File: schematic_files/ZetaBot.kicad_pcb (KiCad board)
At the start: 2 copper layers, 241.5 x 110.5 mm, 17 parts, among them J1 USB C PD Modulle, J2 Conn_01x05, J3 MOTOR_L, J4 MOTOR_R, SW1 SW_SPDT, U1 RPI5, U1 RPLIDAR C1, U2 Buck Converter

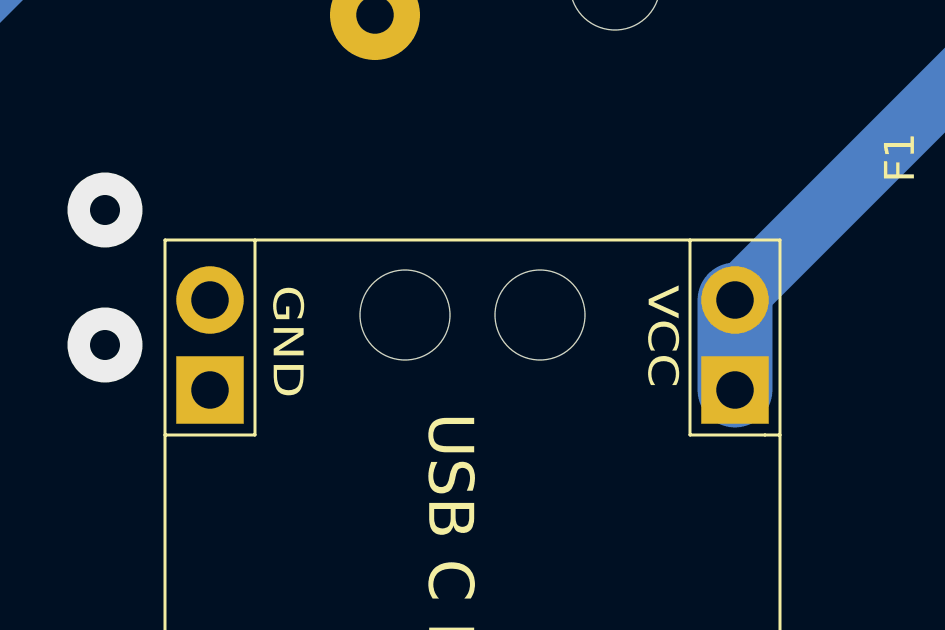
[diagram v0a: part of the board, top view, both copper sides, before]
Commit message: Added a new footprint for the USB C PD.
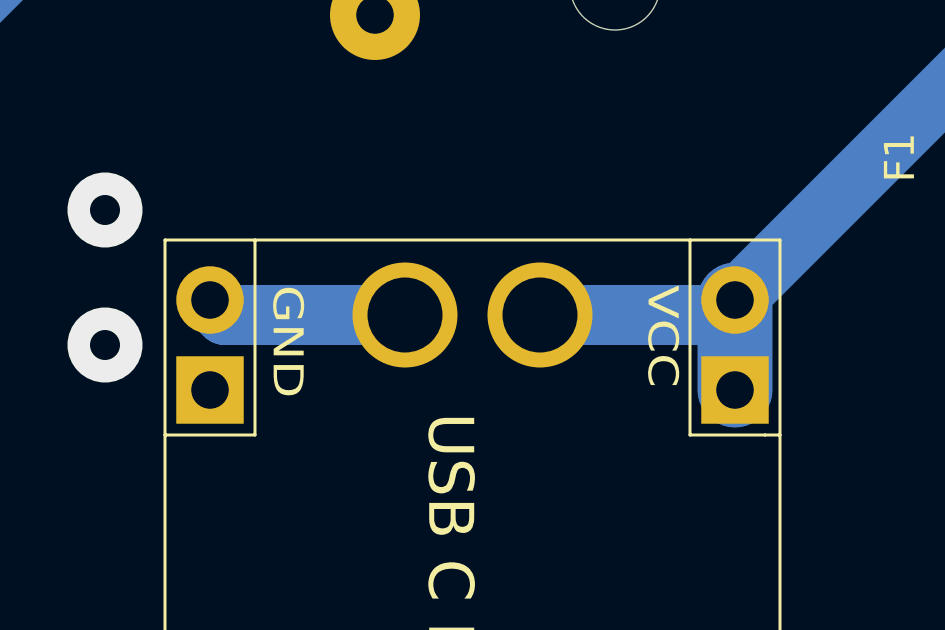
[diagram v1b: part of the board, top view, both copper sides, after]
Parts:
- J1: footprint deltabot:USB_C -> DeltaBotFootprints:USB_C
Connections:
- F1 pad 2: Net-(J1-VCC) -> Net-(F1-Pad2)
- J1 pad 1: Net-(J1-VCC) -> Net-(F1-Pad2)
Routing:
- net Net-(F1-Pad2): track 0.00 -> 27.9 mm
- net Net-(J1-VCC): track 21.2 -> 0.00 mm
- net GND: track 0.00 -> 6.71 mm
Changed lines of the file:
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@@
 		(property ki_fp_filters "CP_*")
 		(sheetname "/")
-		(sheetfile "EpsilonBot.kicad_sch")
+		(sheetfile "ZetaBot.kicad_sch")
 		(units
 			(unit
@@
 		(property ki_fp_filters "Connector*:*_1x??_*")
 		(sheetname "/")
-		(sheetfile "EpsilonBot.kicad_sch")
+		(sheetfile "ZetaBot.kicad_sch")
 		(units
 			(unit
@@
 		)
 		(sheetname "/")
-		(sheetfile "EpsilonBot.kicad_sch")
+		(sheetfile "ZetaBot.kicad_sch")
 		(attr through_hole)
 		(duplicate_pad_numbers_are_jumpers no)
@@
 		(property ki_fp_filters "Connector*:*_1x??_*")
 		(sheetname "/")
-		(sheetfile "EpsilonBot.kicad_sch")
+		(sheetfile "ZetaBot.kicad_sch")
 		(units
 			(unit
@@
 		)
 	)
-	(footprint "deltabot:USB_C"
+	(footprint "DeltaBotFootprints:USB_C"
 		(layer "F.Cu")
 		(at 168.5 130.5 -90)
@@
 		(property ki_fp_filters "USB*C*Receptacle*")
 		(sheetname "/")
-		(sheetfile "EpsilonBot.kicad_sch")
+		(sheetfile "ZetaBot.kicad_sch")
 		(units
 			(unit
 				(name "A")
-				(pins "1" "2")
+				(pins "3" "4" "1" "2")
 			)
 		)
@@
 			)
 		)
-		(pad "" np_thru_hole circle
-			(at -12.5 -2 270)
-			(size 3 3)
-			(drill 3)
-			(layers "*.Cu" "*.Mask")
-		)
-		(pad "" np_thru_hole circle
-			(at -12.5 2.5 270)
-			(size 2.5 2.5)
-			(drill 3)
-			(layers "*.Cu" "*.Mask")
-		)
 		(pad "1" thru_hole circle
 			(at -13 -8.5 270)
@@
 			(layers "*.Cu" "*.Mask")
 			(remove_unused_layers no)
-			(net "Net-(J1-VCC)")
+			(net "Net-(F1-Pad2)")
 			(pinfunction "VCC_1")
-			(pintype "passive")
+			(pintype "power_out")
 			(thermal_bridge_angle 90)
 		)
@@
 			(layers "*.Cu" "*.Mask")
 			(remove_unused_layers no)
-			(net "Net-(J1-VCC)")
+			(net "Net-(F1-Pad2)")
 			(pinfunction "VCC_1")
-			(pintype "passive")
+			(pintype "power_out")
 		)
 		(pad "2" thru_hole circle
@@
 			(net "GND")
 			(pinfunction "GND_2")
-			(pintype "passive")
+			(pintype "power_out")
 			(thermal_bridge_angle 90)
 		)
@@
 			(net "GND")
 			(pinfunction "GND_2")
-			(pintype "passive")
+			(pintype "power_out")
+		)
+		(pad "3" thru_hole circle
+			(at -12.5 -2 270)
+			(size 3.5 3.5)
+			(drill 2.5)
+			(layers "*.Cu" "*.Mask")
+			(remove_unused_layers no)
+			(net "Net-(F1-Pad2)")
+			(pinfunction "VCC_3")
+			(pintype "power_out")
+		)
+		(pad "4" thru_hole circle
+			(at -12.5 2.5 270)
+			(size 3.5 3.5)
+			(drill 2.5)
+			(layers "*.Cu" "*.Mask")
+			(remove_unused_layers no)
+			(net "GND")
+			(pinfunction "GND_4")
+			(pintype "power_out")
 		)
 		(embedded_fonts no)
@@
 		(property ki_fp_filters "CP_*")
 		(sheetname "/")
-		(sheetfile "EpsilonBot.kicad_sch")
+		(sheetfile "ZetaBot.kicad_sch")
 		(units
 			(unit
@@
 		(property ki_fp_filters "LED* LED_SMD:* LED_THT:*")
 		(sheetname "/")
-		(sheetfile "EpsilonBot.kicad_sch")
+		(sheetfile "ZetaBot.kicad_sch")
 		(units
 			(unit
@@
 		(property ki_fp_filters "Connector*:*_1x??_*")
 		(sheetname "/")
-		(sheetfile "EpsilonBot.kicad_sch")
+		(sheetfile "ZetaBot.kicad_sch")
 		(units
 			(unit
@@
 		(property ki_fp_filters "R_*")
 		(sheetname "/")
-		(sheetfile "EpsilonBot.kicad_sch")
+		(sheetfile "ZetaBot.kicad_sch")
 		(units
 			(unit
@@
 		(property ki_fp_filters "CP_*")
 		(sheetname "/")
-		(sheetfile "EpsilonBot.kicad_sch")
+		(sheetfile "ZetaBot.kicad_sch")
 		(units
 			(unit
@@
 		(property ki_fp_filters "CP_*")
 		(sheetname "/")
-		(sheetfile "EpsilonBot.kicad_sch")
+		(sheetfile "ZetaBot.kicad_sch")
 		(units
 			(unit
@@
 		(property ki_fp_filters "*Fuse*")
 		(sheetname "/")
-		(sheetfile "EpsilonBot.kicad_sch")
+		(sheetfile "ZetaBot.kicad_sch")
 		(units
 			(unit
@@
 			(layers "*.Cu" "*.Mask")
 			(remove_unused_layers no)
-			(net "Net-(J1-VCC)")
+			(net "Net-(F1-Pad2)")
 			(pintype "passive")
 		)
@@
 		)
 		(sheetname "/")
-		(sheetfile "EpsilonBot.kicad_sch")
+		(sheetfile "ZetaBot.kicad_sch")
 		(units
 			(unit
@@
 		(property ki_fp_filters "CP_*")
 		(sheetname "/")
-		(sheetfile "EpsilonBot.kicad_sch")
+		(sheetfile "ZetaBot.kicad_sch")
 		(units
 			(unit
@@
 		(property ki_fp_filters "CP_*")
 		(sheetname "/")
-		(sheetfile "EpsilonBot.kicad_sch")
+		(sheetfile "ZetaBot.kicad_sch")
 		(units
 			(unit
@@
 		)
 		(sheetname "/")
-		(sheetfile "EpsilonBot.kicad_sch")
+		(sheetfile "ZetaBot.kicad_sch")
 		(units
 			(unit
@@
 	)
 	(segment
+		(start 166 118)
+		(end 160 118)
+		(width 2)
+		(layer "B.Cu")
+		(net "GND")
+	)
+	(segment
+		(start 160 118)
+		(end 159.5 117.5)
+		(width 2)
+		(layer "B.Cu")
+		(net "GND")
+	)
+	(segment
 		(start 46.4 134.2)
 		(end 47.6 135.4)
@@
 	)
 	(segment
-		(start 177 117.5)
-		(end 177 120.5)
-		(width 2.5)
-		(layer "B.Cu")
-		(net "Net-(J1-VCC)")
-	)
-	(segment
-		(start 189.5 104.5)
-		(end 189.5 105)
-		(width 2)
-		(layer "B.Cu")
-		(net "Net-(J1-VCC)")
-	)
-	(segment
-		(start 189.5 105)
-		(end 177 117.5)
-		(width 2)
-		(layer "B.Cu")
-		(net "Net-(J1-VCC)")
-	)
-	(segment
 		(start 190.845 91.08)
 		(end 190.765 91)
@@
 		(net "Net-(SW1-B)")
 	)
+	(segment
+		(start 177 117.5)
+		(end 177 120.5)
+		(width 2.5)
+		(layer "B.Cu")
+		(net "Net-(F1-Pad2)")
+	)
+	(segment
+		(start 189.5 104.5)
+		(end 189.5 105)
+		(width 2)
+		(layer "B.Cu")
+		(net "Net-(F1-Pad2)")
+	)
+	(segment
+		(start 189.5 105)
+		(end 177 117.5)
+		(width 2)
+		(layer "B.Cu")
+		(net "Net-(F1-Pad2)")
+	)
+	(segment
+		(start 176.5 118)
+		(end 177 117.5)
+		(width 2)
+		(layer "B.Cu")
+		(net "Net-(F1-Pad2)")
+	)
+	(segment
+		(start 170.5 118)
+		(end 176.5 118)
+		(width 2)
+		(layer "B.Cu")
+		(net "Net-(F1-Pad2)")
+	)
 	(zone
